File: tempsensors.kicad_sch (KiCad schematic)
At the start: 22 parts, among them J3 TSM-102-01-L-SV, J4 TSM-102-01-L-SV, U10 ADS7142IRUGR, U11 MCP9808T-E_MC, U9 MCP9808T-E_MC

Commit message: work on control logic
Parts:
- renumbered C14 to C16, C15 to C17, C16 to C18, C17 to C19, C18 to C20, C19 to C21, C20 to C22, C21 to C23, R37 to R40, R38 to R41, R39 to R42, R40 to R43, R41 to R44, R42 to R45, R43 to R46, R44 to R47, R45 to R48, U9 to U10, U10 to U11, U11 to U12
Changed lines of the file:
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@@
   (symbol (lib_id "Device:C_Small") (at 137.795 147.32 0) (unit 1)
     (in_bom yes) (on_board yes) (fields_autoplaced)
-    (property "Reference" "C18" (id 0) (at 140.97 146.0562 0)
+    (property "Reference" "C20" (id 0) (at 140.97 146.0562 0)
       (effects (font (size 1.27 1.27)) (justify left))
     )
@@
   (symbol (lib_id "Sensor_I2C_Microchip:MCP9808T-E_MC") (at 215.265 85.09 0) (mirror y) (unit 1)
     (in_bom yes) (on_board yes)
-    (property "Reference" "U11" (id 0) (at 205.105 73.66 0)
+    (property "Reference" "U12" (id 0) (at 205.105 73.66 0)
       (effects (font (size 1.27 1.27)) (justify left))
     )
@@
   (symbol (lib_id "power:GND") (at 121.285 100.33 0) (unit 1)
     (in_bom yes) (on_board yes) (fields_autoplaced)
-    (property "Reference" "#PWR027" (id 0) (at 121.285 106.68 0)
+    (property "Reference" "#PWR028" (id 0) (at 121.285 106.68 0)
       (effects (font (size 1.27 1.27)) hide)
     )
@@
   (symbol (lib_id "Device:R_Small") (at 151.765 147.32 0) (unit 1)
     (in_bom yes) (on_board yes) (fields_autoplaced)
-    (property "Reference" "R41" (id 0) (at 153.67 146.0499 0)
+    (property "Reference" "R44" (id 0) (at 153.67 146.0499 0)
       (effects (font (size 1.27 1.27)) (justify left))
     )
@@
   (symbol (lib_id "power:GND") (at 197.485 101.6 0) (mirror y) (unit 1)
     (in_bom yes) (on_board yes)
-    (property "Reference" "#PWR030" (id 0) (at 197.485 107.95 0)
+    (property "Reference" "#PWR031" (id 0) (at 197.485 107.95 0)
       (effects (font (size 1.27 1.27)) hide)
     )
@@
   (symbol (lib_id "Device:C_Small") (at 51.435 68.58 0) (mirror y) (unit 1)
     (in_bom yes) (on_board yes) (fields_autoplaced)
-    (property "Reference" "C16" (id 0) (at 48.895 67.31 0)
+    (property "Reference" "C18" (id 0) (at 48.895 67.31 0)
       (effects (font (size 1.27 1.27)) (justify left))
     )
@@
   (symbol (lib_name "MCP9808T-E_MC_1") (lib_id "Sensor_I2C_Microchip:MCP9808T-E_MC") (at 84.455 83.82 0) (mirror y) (unit 1)
     (in_bom yes) (on_board yes)
-    (property "Reference" "U9" (id 0) (at 74.295 72.39 0)
+    (property "Reference" "U10" (id 0) (at 74.295 72.39 0)
       (effects (font (size 1.27 1.27)) (justify left))
     )
@@
   (symbol (lib_id "Analog_ADC_TI:ADS7142IRUGR") (at 107.95 149.225 0) (unit 1)
     (in_bom yes) (on_board yes)
-    (property "Reference" "U10" (id 0) (at 88.9 132.715 0)
+    (property "Reference" "U11" (id 0) (at 88.9 132.715 0)
       (effects (font (size 1.524 1.524)))
     )
@@
   (symbol (lib_id "Device:C_Small") (at 182.245 69.85 0) (mirror y) (unit 1)
     (in_bom yes) (on_board yes) (fields_autoplaced)
-    (property "Reference" "C21" (id 0) (at 179.705 68.58 0)
+    (property "Reference" "C23" (id 0) (at 179.705 68.58 0)
       (effects (font (size 1.27 1.27)) (justify left))
     )
@@
   (symbol (lib_id "power:GND") (at 40.005 76.2 0) (mirror y) (unit 1)
     (in_bom yes) (on_board yes)
-    (property "Reference" "#PWR024" (id 0) (at 40.005 82.55 0)
+    (property "Reference" "#PWR025" (id 0) (at 40.005 82.55 0)
       (effects (font (size 1.27 1.27)) hide)
     )
@@
   (symbol (lib_id "Device:R_Small") (at 245.745 90.17 90) (unit 1)
     (in_bom yes) (on_board yes)
-    (property "Reference" "R44" (id 0) (at 240.665 88.9 90))
+    (property "Reference" "R47" (id 0) (at 240.665 88.9 90))
     (property "Value" "1k" (id 1) (at 249.555 88.9 90))
     (property "Footprint" "Resistor_SMD:R_0402_1005Metric" (id 2) (at 245.745 90.17 0)
@@
   (symbol (lib_id "Device:R_Small") (at 245.745 92.71 90) (unit 1)
     (in_bom yes) (on_board yes)
-    (property "Reference" "R45" (id 0) (at 240.665 91.44 90))
+    (property "Reference" "R48" (id 0) (at 240.665 91.44 90))
     (property "Value" "1k" (id 1) (at 249.555 91.44 90))
     (property "Footprint" "Resistor_SMD:R_0402_1005Metric" (id 2) (at 245.745 92.71 0)
@@
   (symbol (lib_id "power:GND") (at 170.815 77.47 0) (mirror y) (unit 1)
     (in_bom yes) (on_board yes)
-    (property "Reference" "#PWR029" (id 0) (at 170.815 83.82 0)
+    (property "Reference" "#PWR030" (id 0) (at 170.815 83.82 0)
       (effects (font (size 1.27 1.27)) hide)
     )
@@
   (symbol (lib_id "Device:R_Small") (at 114.935 86.36 90) (unit 1)
     (in_bom yes) (on_board yes)
-    (property "Reference" "R38" (id 0) (at 109.855 85.09 90))
+    (property "Reference" "R41" (id 0) (at 109.855 85.09 90))
     (property "Value" "1k" (id 1) (at 118.745 85.09 90))
     (property "Footprint" "Resistor_SMD:R_0402_1005Metric" (id 2) (at 114.935 86.36 0)
@@
   (symbol (lib_id "power:GND") (at 252.095 101.6 0) (mirror y) (unit 1)
     (in_bom yes) (on_board yes)
-    (property "Reference" "#PWR031" (id 0) (at 252.095 107.95 0)
+    (property "Reference" "#PWR032" (id 0) (at 252.095 107.95 0)
       (effects (font (size 1.27 1.27)) hide)
     )
@@
   (symbol (lib_id "Device:C_Small") (at 137.795 167.64 0) (unit 1)
     (in_bom yes) (on_board yes) (fields_autoplaced)
-    (property "Reference" "C19" (id 0) (at 140.97 166.3762 0)
+    (property "Reference" "C21" (id 0) (at 140.97 166.3762 0)
       (effects (font (size 1.27 1.27)) (justify left))
     )
@@
   (symbol (lib_id "Device:C_Small") (at 48.26 137.16 0) (unit 1)
     (in_bom yes) (on_board yes) (fields_autoplaced)
-    (property "Reference" "C15" (id 0) (at 51.435 135.8962 0)
+    (property "Reference" "C17" (id 0) (at 51.435 135.8962 0)
       (effects (font (size 1.27 1.27)) (justify left))
     )
@@
   (symbol (lib_id "Device:R_Small") (at 245.745 87.63 90) (unit 1)
     (in_bom yes) (on_board yes)
-    (property "Reference" "R43" (id 0) (at 240.665 86.36 90))
+    (property "Reference" "R46" (id 0) (at 240.665 86.36 90))
     (property "Value" "1k" (id 1) (at 249.555 86.36 90))
     (property "Footprint" "Resistor_SMD:R_0402_1005Metric" (id 2) (at 245.745 87.63 0)
@@
   (symbol (lib_id "Device:R_Small") (at 151.765 167.64 0) (unit 1)
     (in_bom yes) (on_board yes) (fields_autoplaced)
-    (property "Reference" "R42" (id 0) (at 153.67 166.3699 0)
+    (property "Reference" "R45" (id 0) (at 153.67 166.3699 0)
       (effects (font (size 1.27 1.27)) (justify left))
     )
@@
   (symbol (lib_id "power:GND") (at 164.465 177.165 0) (unit 1)
     (in_bom yes) (on_board yes) (fields_autoplaced)
-    (property "Reference" "#PWR028" (id 0) (at 164.465 183.515 0)
+    (property "Reference" "#PWR029" (id 0) (at 164.465 183.515 0)
       (effects (font (size 1.27 1.27)) hide)
     )
@@
   (symbol (lib_id "Device:R_Small") (at 69.215 137.16 0) (unit 1)
     (in_bom yes) (on_board yes) (fields_autoplaced)
-    (property "Reference" "R37" (id 0) (at 71.12 135.8899 0)
+    (property "Reference" "R40" (id 0) (at 71.12 135.8899 0)
       (effects (font (size 1.27 1.27)) (justify left))
     )
@@
   (symbol (lib_id "power:GND") (at 48.26 177.165 0) (unit 1)
     (in_bom yes) (on_board yes) (fields_autoplaced)
-    (property "Reference" "#PWR025" (id 0) (at 48.26 183.515 0)
+    (property "Reference" "#PWR026" (id 0) (at 48.26 183.515 0)
       (effects (font (size 1.27 1.27)) hide)
     )
@@
   (symbol (lib_id "Device:R_Small") (at 114.935 91.44 90) (unit 1)
     (in_bom yes) (on_board yes)
-    (property "Reference" "R40" (id 0) (at 109.855 90.17 90))
+    (property "Reference" "R43" (id 0) (at 109.855 90.17 90))
     (property "Value" "1k" (id 1) (at 118.745 90.17 90))
     (property "Footprint" "Resistor_SMD:R_0402_1005Metric" (id 2) (at 114.935 91.44 0)
@@
   (symbol (lib_id "Device:C_Small") (at 40.005 68.58 0) (mirror y) (unit 1)
     (in_bom yes) (on_board yes) (fields_autoplaced)
-    (property "Reference" "C14" (id 0) (at 37.465 67.31 0)
+    (property "Reference" "C16" (id 0) (at 37.465 67.31 0)
       (effects (font (size 1.27 1.27)) (justify left))
     )
@@
   (symbol (lib_id "Device:C_Small") (at 170.815 69.85 0) (mirror y) (unit 1)
     (in_bom yes) (on_board yes) (fields_autoplaced)
-    (property "Reference" "C20" (id 0) (at 168.275 68.58 0)
+    (property "Reference" "C22" (id 0) (at 168.275 68.58 0)
       (effects (font (size 1.27 1.27)) (justify left))
     )
@@
   (symbol (lib_id "Device:C_Small") (at 58.42 137.16 0) (unit 1)
     (in_bom yes) (on_board yes) (fields_autoplaced)
-    (property "Reference" "C17" (id 0) (at 61.595 135.8962 0)
+    (property "Reference" "C19" (id 0) (at 61.595 135.8962 0)
       (effects (font (size 1.27 1.27)) (justify left))
     )
@@
   (symbol (lib_id "power:GND") (at 66.675 100.33 0) (unit 1)
     (in_bom yes) (on_board yes) (fields_autoplaced)
-    (property "Reference" "#PWR026" (id 0) (at 66.675 106.68 0)
+    (property "Reference" "#PWR027" (id 0) (at 66.675 106.68 0)
       (effects (font (size 1.27 1.27)) hide)
     )
@@
   (symbol (lib_id "Device:R_Small") (at 114.935 88.9 90) (unit 1)
     (in_bom yes) (on_board yes)
-    (property "Reference" "R39" (id 0) (at 109.855 87.63 90))
+    (property "Reference" "R42" (id 0) (at 109.855 87.63 90))
     (property "Value" "1k" (id 1) (at 118.745 87.63 90))
     (property "Footprint" "Resistor_SMD:R_0402_1005Metric" (id 2) (at 114.935 88.9 0)

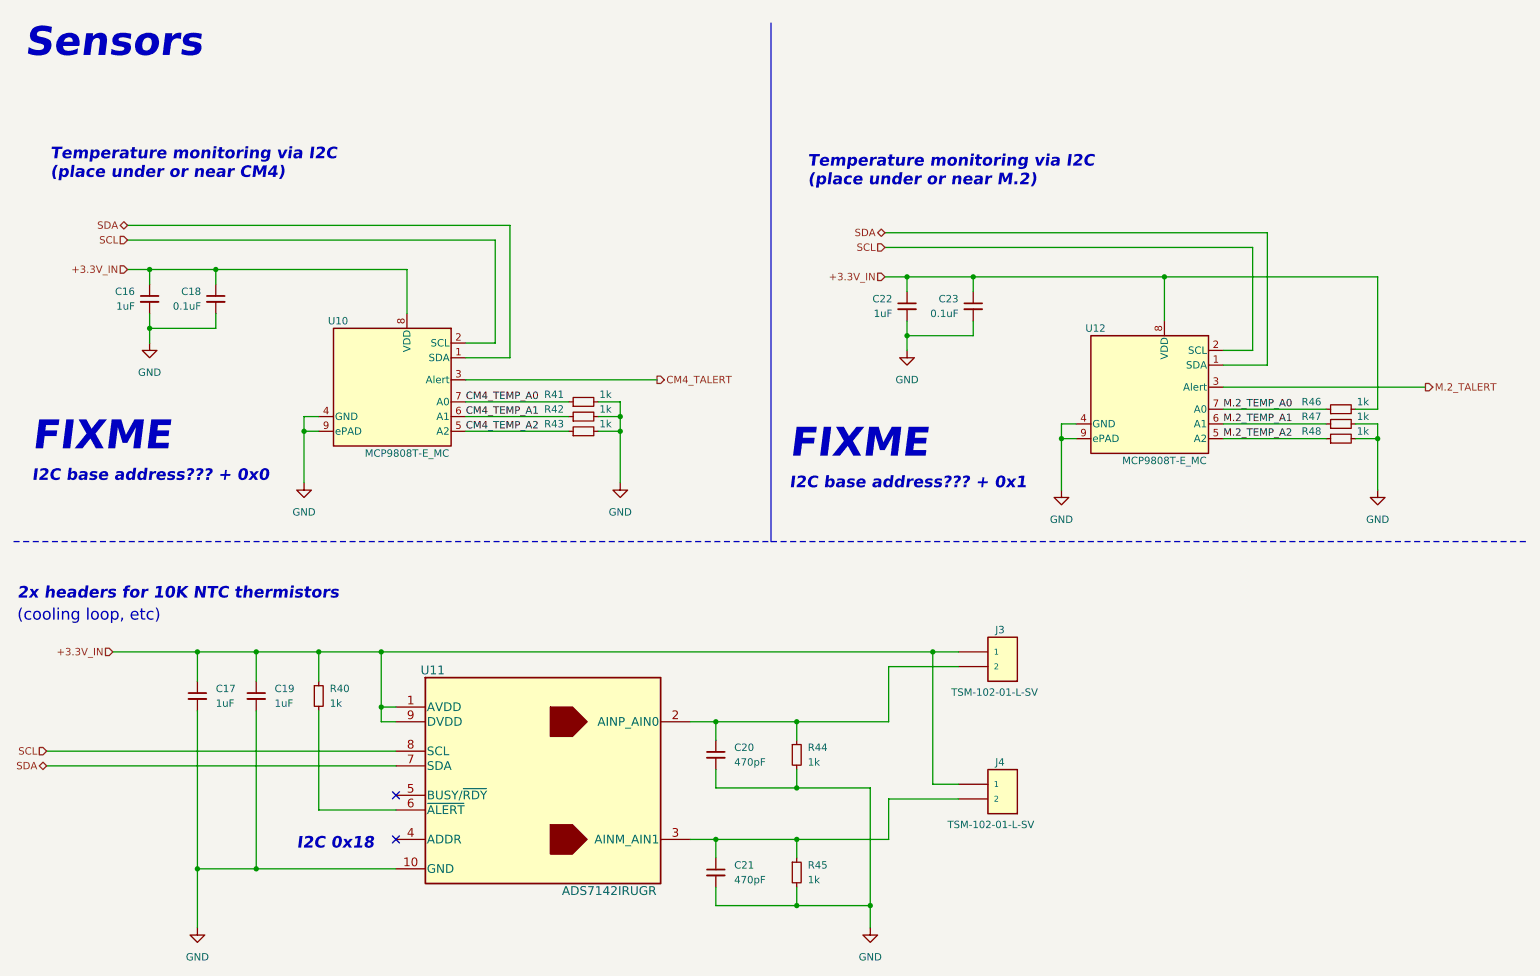
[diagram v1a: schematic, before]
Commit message: connecterized faceplate, refreshed schematic
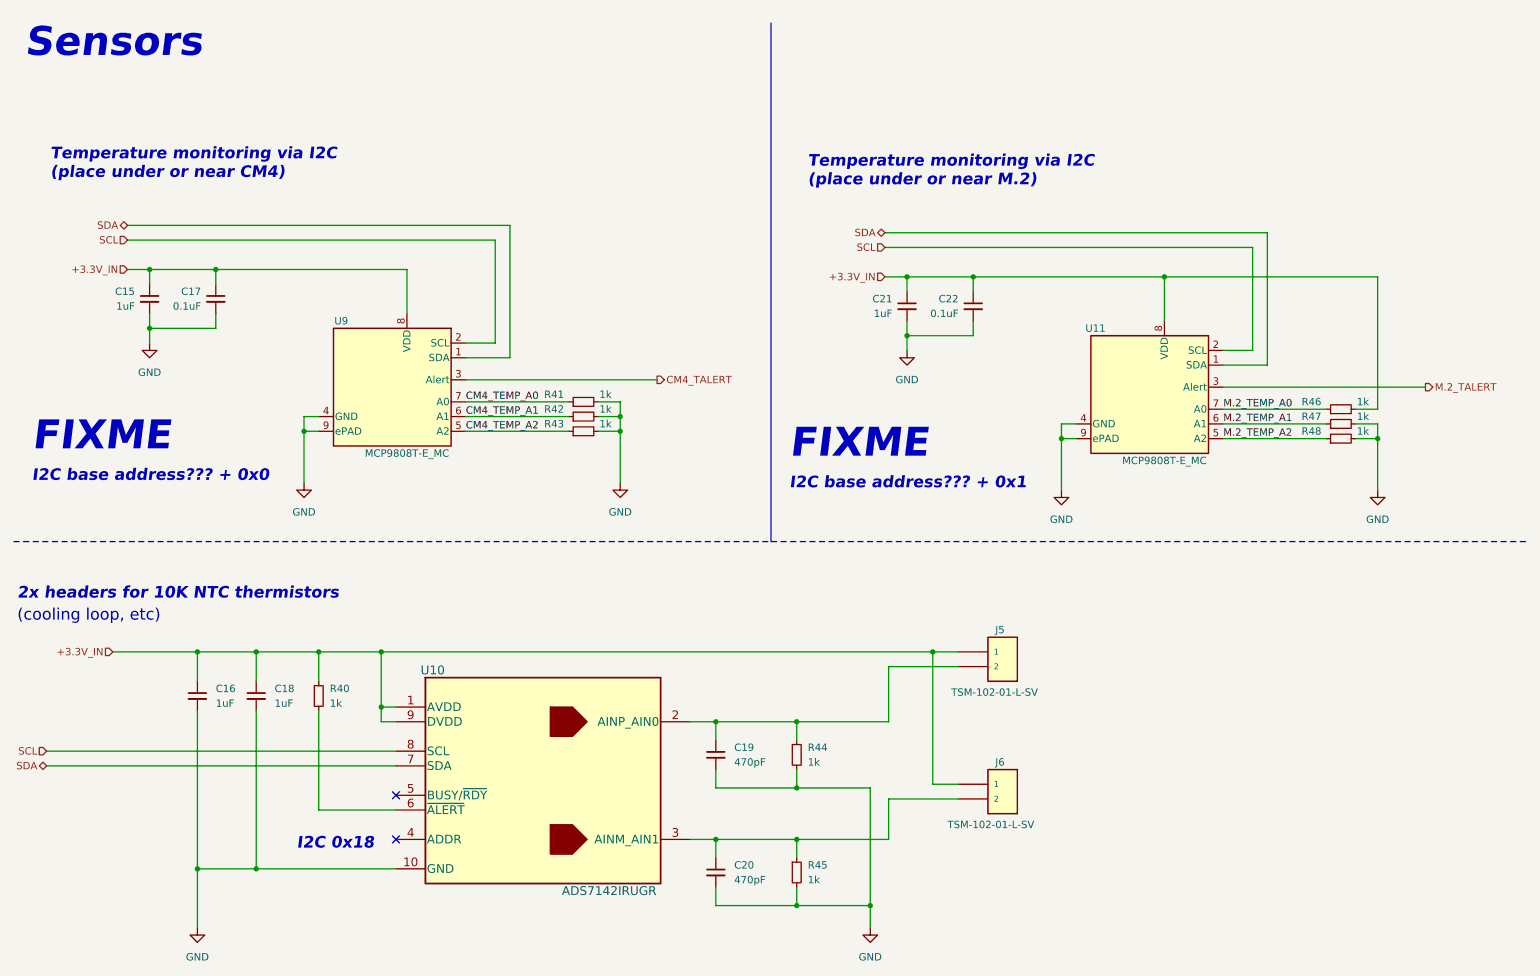
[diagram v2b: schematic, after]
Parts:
- renumbered C16 to C15, C17 to C16, C18 to C17, C19 to C18, C20 to C19, C21 to C20, C22 to C21, C23 to C22, J3 to J5, J4 to J6, U11 to U10, U12 to U11, U10 to U9
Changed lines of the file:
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@@
   (symbol (lib_id "Device:C_Small") (at 137.795 147.32 0) (unit 1)
     (in_bom yes) (on_board yes) (fields_autoplaced)
-    (property "Reference" "C20" (id 0) (at 140.97 146.0562 0)
+    (property "Reference" "C19" (id 0) (at 140.97 146.0562 0)
       (effects (font (size 1.27 1.27)) (justify left))
     )
@@
   (symbol (lib_id "Sensor_I2C_Microchip:MCP9808T-E_MC") (at 215.265 85.09 0) (mirror y) (unit 1)
     (in_bom yes) (on_board yes)
-    (property "Reference" "U12" (id 0) (at 205.105 73.66 0)
+    (property "Reference" "U11" (id 0) (at 205.105 73.66 0)
       (effects (font (size 1.27 1.27)) (justify left))
     )
@@
   (symbol (lib_id "power:GND") (at 121.285 100.33 0) (unit 1)
     (in_bom yes) (on_board yes) (fields_autoplaced)
-    (property "Reference" "#PWR028" (id 0) (at 121.285 106.68 0)
+    (property "Reference" "#PWR027" (id 0) (at 121.285 106.68 0)
       (effects (font (size 1.27 1.27)) hide)
     )
@@
   (symbol (lib_id "power:GND") (at 197.485 101.6 0) (mirror y) (unit 1)
     (in_bom yes) (on_board yes)
-    (property "Reference" "#PWR031" (id 0) (at 197.485 107.95 0)
+    (property "Reference" "#PWR030" (id 0) (at 197.485 107.95 0)
       (effects (font (size 1.27 1.27)) hide)
     )
@@
   (symbol (lib_id "Device:C_Small") (at 51.435 68.58 0) (mirror y) (unit 1)
     (in_bom yes) (on_board yes) (fields_autoplaced)
-    (property "Reference" "C18" (id 0) (at 48.895 67.31 0)
+    (property "Reference" "C17" (id 0) (at 48.895 67.31 0)
       (effects (font (size 1.27 1.27)) (justify left))
     )
@@
   (symbol (lib_id "Connector_Header_Samtec:TSM-102-01-L-SV") (at 187.325 129.54 0) (mirror y) (unit 1)
     (in_bom yes) (on_board yes)
-    (property "Reference" "J3" (id 0) (at 186.055 125.73 0)
+    (property "Reference" "J5" (id 0) (at 186.055 125.73 0)
       (effects (font (size 1.27 1.27)) (justify right))
     )
@@
   (symbol (lib_name "MCP9808T-E_MC_1") (lib_id "Sensor_I2C_Microchip:MCP9808T-E_MC") (at 84.455 83.82 0) (mirror y) (unit 1)
     (in_bom yes) (on_board yes)
-    (property "Reference" "U10" (id 0) (at 74.295 72.39 0)
+    (property "Reference" "U9" (id 0) (at 74.295 72.39 0)
       (effects (font (size 1.27 1.27)) (justify left))
     )
@@
   (symbol (lib_id "Analog_ADC_TI:ADS7142IRUGR") (at 107.95 149.225 0) (unit 1)
     (in_bom yes) (on_board yes)
-    (property "Reference" "U11" (id 0) (at 88.9 132.715 0)
+    (property "Reference" "U10" (id 0) (at 88.9 132.715 0)
       (effects (font (size 1.524 1.524)))
     )
@@
   (symbol (lib_id "Device:C_Small") (at 182.245 69.85 0) (mirror y) (unit 1)
     (in_bom yes) (on_board yes) (fields_autoplaced)
-    (property "Reference" "C23" (id 0) (at 179.705 68.58 0)
+    (property "Reference" "C22" (id 0) (at 179.705 68.58 0)
       (effects (font (size 1.27 1.27)) (justify left))
     )
@@
   (symbol (lib_id "power:GND") (at 40.005 76.2 0) (mirror y) (unit 1)
     (in_bom yes) (on_board yes)
-    (property "Reference" "#PWR025" (id 0) (at 40.005 82.55 0)
+    (property "Reference" "#PWR024" (id 0) (at 40.005 82.55 0)
       (effects (font (size 1.27 1.27)) hide)
     )
@@
   (symbol (lib_id "Connector_Header_Samtec:TSM-102-01-L-SV") (at 187.325 152.4 0) (mirror y) (unit 1)
     (in_bom yes) (on_board yes)
-    (property "Reference" "J4" (id 0) (at 186.055 148.59 0)
+    (property "Reference" "J6" (id 0) (at 186.055 148.59 0)
       (effects (font (size 1.27 1.27)) (justify right))
     )
@@
   (symbol (lib_id "power:GND") (at 170.815 77.47 0) (mirror y) (unit 1)
     (in_bom yes) (on_board yes)
-    (property "Reference" "#PWR030" (id 0) (at 170.815 83.82 0)
+    (property "Reference" "#PWR029" (id 0) (at 170.815 83.82 0)
       (effects (font (size 1.27 1.27)) hide)
     )
@@
   (symbol (lib_id "power:GND") (at 252.095 101.6 0) (mirror y) (unit 1)
     (in_bom yes) (on_board yes)
-    (property "Reference" "#PWR032" (id 0) (at 252.095 107.95 0)
+    (property "Reference" "#PWR031" (id 0) (at 252.095 107.95 0)
       (effects (font (size 1.27 1.27)) hide)
     )
@@
   (symbol (lib_id "Device:C_Small") (at 137.795 167.64 0) (unit 1)
     (in_bom yes) (on_board yes) (fields_autoplaced)
-    (property "Reference" "C21" (id 0) (at 140.97 166.3762 0)
+    (property "Reference" "C20" (id 0) (at 140.97 166.3762 0)
       (effects (font (size 1.27 1.27)) (justify left))
     )
@@
   (symbol (lib_id "Device:C_Small") (at 48.26 137.16 0) (unit 1)
     (in_bom yes) (on_board yes) (fields_autoplaced)
-    (property "Reference" "C17" (id 0) (at 51.435 135.8962 0)
+    (property "Reference" "C16" (id 0) (at 51.435 135.8962 0)
       (effects (font (size 1.27 1.27)) (justify left))
     )
@@
   (symbol (lib_id "power:GND") (at 164.465 177.165 0) (unit 1)
     (in_bom yes) (on_board yes) (fields_autoplaced)
-    (property "Reference" "#PWR029" (id 0) (at 164.465 183.515 0)
+    (property "Reference" "#PWR028" (id 0) (at 164.465 183.515 0)
       (effects (font (size 1.27 1.27)) hide)
     )
@@
   (symbol (lib_id "power:GND") (at 48.26 177.165 0) (unit 1)
     (in_bom yes) (on_board yes) (fields_autoplaced)
-    (property "Reference" "#PWR026" (id 0) (at 48.26 183.515 0)
+    (property "Reference" "#PWR025" (id 0) (at 48.26 183.515 0)
       (effects (font (size 1.27 1.27)) hide)
     )
@@
   (symbol (lib_id "Device:C_Small") (at 40.005 68.58 0) (mirror y) (unit 1)
     (in_bom yes) (on_board yes) (fields_autoplaced)
-    (property "Reference" "C16" (id 0) (at 37.465 67.31 0)
+    (property "Reference" "C15" (id 0) (at 37.465 67.31 0)
       (effects (font (size 1.27 1.27)) (justify left))
     )
@@
   (symbol (lib_id "Device:C_Small") (at 170.815 69.85 0) (mirror y) (unit 1)
     (in_bom yes) (on_board yes) (fields_autoplaced)
-    (property "Reference" "C22" (id 0) (at 168.275 68.58 0)
+    (property "Reference" "C21" (id 0) (at 168.275 68.58 0)
       (effects (font (size 1.27 1.27)) (justify left))
     )
@@
   (symbol (lib_id "Device:C_Small") (at 58.42 137.16 0) (unit 1)
     (in_bom yes) (on_board yes) (fields_autoplaced)
-    (property "Reference" "C19" (id 0) (at 61.595 135.8962 0)
+    (property "Reference" "C18" (id 0) (at 61.595 135.8962 0)
       (effects (font (size 1.27 1.27)) (justify left))
     )
@@
   (symbol (lib_id "power:GND") (at 66.675 100.33 0) (unit 1)
     (in_bom yes) (on_board yes) (fields_autoplaced)
-    (property "Reference" "#PWR027" (id 0) (at 66.675 106.68 0)
-      (effects (font (size 1.27 1.27)) hide)
-    )
+    (property "Reference" "#PWR026" (id 0) (at 66.675 106.68 0)
+      (effects (font (size 1.27 1.27)) hide)
+    )
